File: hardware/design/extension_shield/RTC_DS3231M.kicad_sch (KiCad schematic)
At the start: 8 parts, among them U1 DS3231M

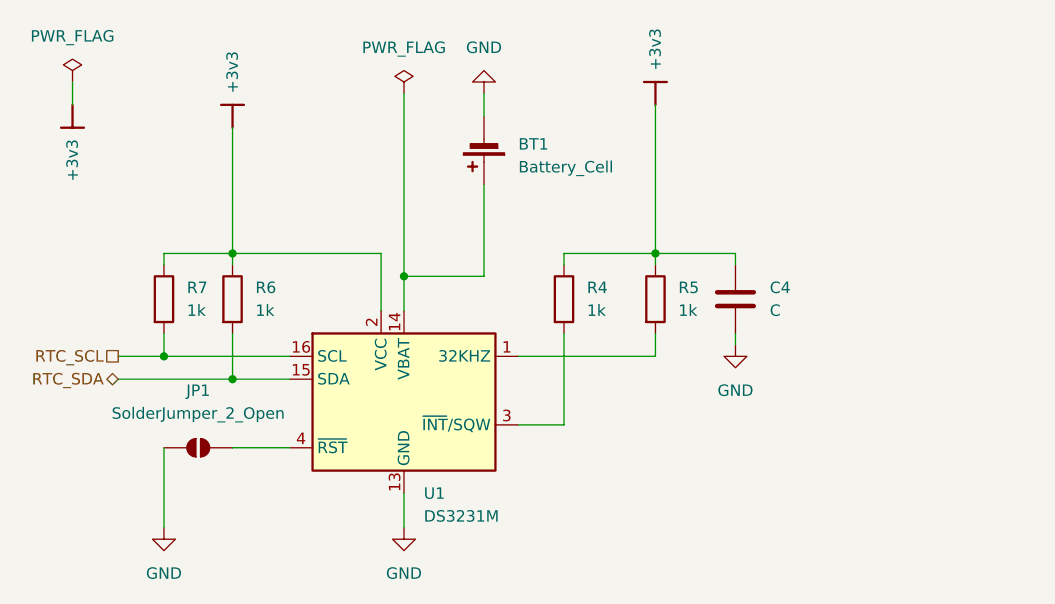
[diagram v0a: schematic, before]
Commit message: [HW/SHIELD] Adds Genereated PDF Schematic & Newer Version of Expansion Shield.
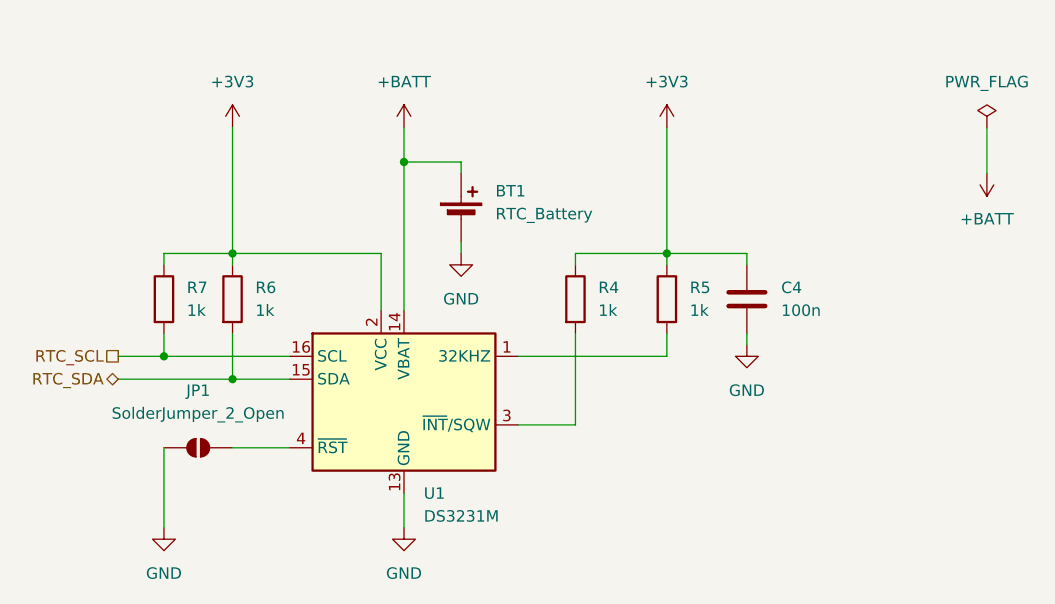
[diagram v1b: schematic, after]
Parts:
- BT1: value Battery_Cell -> RTC_Battery
- C4: value C -> 100n
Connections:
- net +BATT: now reaches BT1.1 (+), U1.14 (VBAT)
- net +3v3 renamed +3V3
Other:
- title: (none) -> Datalogger Expansion Shield
- moved on the sheet: BT1, C4, R4, R5
